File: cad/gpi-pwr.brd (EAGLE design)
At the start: 133 x 73.5 mm, 102 parts, among them CN1 HEADER-1X2, CN2 HEADER-3X1, CN3 HEADER-1X2.4, Q1 MOSFETTO247REV, Q3 MOSFETTO247REV, Q5 MOSFETTO247REV, Q6 MOSFETTO247REV, Q7 MOSFETTO247REV, Q8 MOSFETTO247REV, U1 ACS709, U10 LM61, U11 MAX4452, U12 MAX4452, U2 ACS709, U3 ACPL-P346P346, U4 ACPL-P346P346, U5 ACPL-P346P346, U6 ACPL-P346P346, U7 ACPL-P346P346, U8 ACPL-P346P346, U9 LM61

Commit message: planes
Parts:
- removed Z1: SHORT, jaw:SHORT
- added C29, C30: .1u, jaw:SMD0603
- moved C23 7.07 mm to (38.0, 12.0), turned to 180 degrees
- moved C20 1.30 mm to (80.7, 15.5)
- moved U10 1.04 mm to (80.5, 12.8)
- moved C24 0.51 mm to (38.0, 10.0)
- moved C6 0.30 mm to (112.0, 41.5)
- moved C7 0.30 mm to (112.0, 64.0)
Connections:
- removed net GNDA: C10.1, C11.1, C12.2, C19.2, C20.2, C23.2, C24.2, C25.2, C27.2, C28.2, C5.1, C8.1, C9.2, R10.2, R5.1, U1.15, U1.22, U10.3, U11.2, U12.2, U2.15, U2.22, U9.3, Z1.P$1
- removed net N$32: J2.7
- removed net N$45: J2.8
- removed net N$49: J3.8
- removed net N$53: J3.7
- net GNDM: now also C10.1, C11.1, C12.2, C19.2, C20.2, C23.2, C24.2, C25.2, C27.2, C28.2, C29.2, C30.2, C5.1, C8.1, C9.2, J2.7, J2.8, J3.7, J3.8, R10.2, R5.1, U1.15, U1.22, U10.3, U11.2, U12.2, U2.15, U2.22, U9.3; no longer Z1.P$2
- net VCC: now also C29.1, C30.1
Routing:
- net GNDA: track 115.1 -> 0.00 mm, vias 20 -> 0
- net VCC: track 195.6 -> 109.1 mm, vias 3 -> 6
- net GNDM: track 46.0 -> 128.5 mm, vias 44 -> 39
- net GND: track 100.6 -> 148.1 mm, vias 8 -> 9
- net N$4: track 133.6 -> 143.3 mm
- net V1KDC: track 146.5 -> 147.7 mm
- net ADC5: track 15.3 -> 16.3 mm, vias 0 -> 1
- net N$25: track 104.2 -> 103.3 mm, vias 8 -> 5
- net N$24: track 83.1 -> 82.5 mm
- net N$16: track 101.7 -> 102.2 mm, vias 11 -> 0
- added copper zone on layer 15, net N$4
- added copper zone on layer 15, net VCC
- removed copper zone on layer 15, net GNDA
- removed copper zone on layer 2, net GNDA

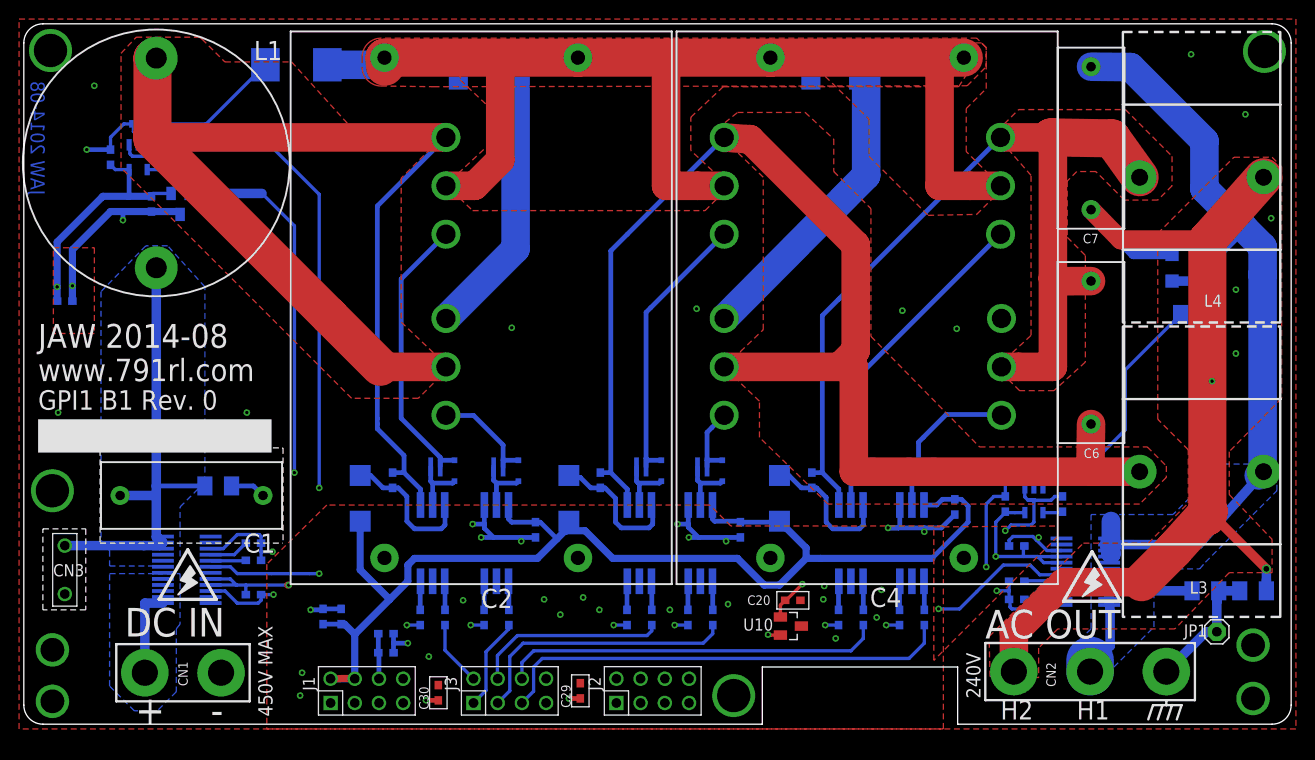
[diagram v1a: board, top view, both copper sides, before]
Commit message: output filter
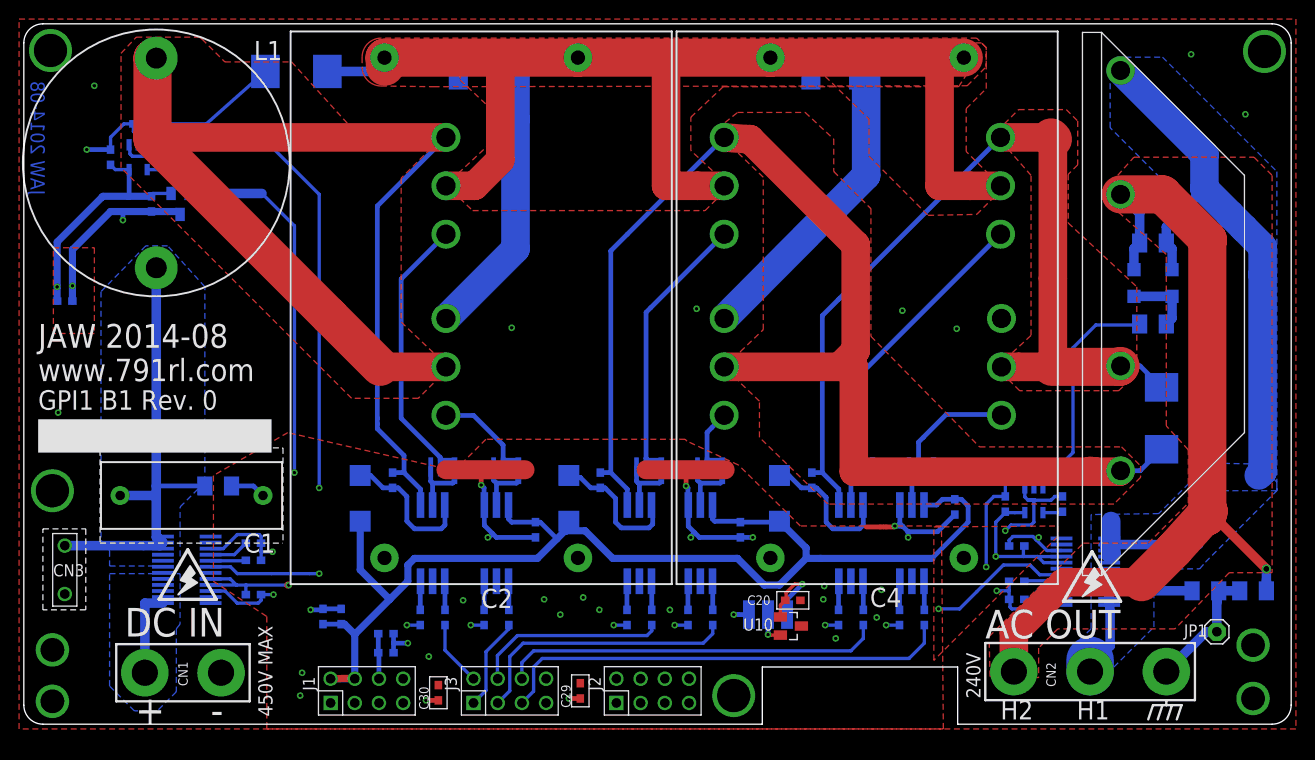
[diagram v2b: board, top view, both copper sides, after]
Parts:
- removed C7: .47u, jaw:R46KI333000N1M
- removed L3, L4: 15u, jaw:BOURNS2303
- added CN4: HEADER-3X12MM, jaw:HEADER-3X1-2SMD
- added R28: 1M, jaw:SMD1206
- added R29: 2M 2kV, jaw:SMD2512
- added Z1, Z2, Z3: SHORT, jaw:SHORT
- C6: value .47u -> FILTER; device jaw:R46KI333000N1M -> jaw-brd:FILTER-B4R0
- moved C6 8.21 mm to (115.1, 49.1)
- moved R12 4.41 mm to (118.5, 44.5)
- moved D2 4.31 mm to (116.5, 48.8)
- moved D1 4.03 mm to (120.5, 48.8)
- moved R1 0.70 mm to (28.6, 71.0)
- moved U$4 0.14 mm to (74.7, 70.8)
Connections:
- net ADC5: now also CN4.2
- net GND: now also C13.2, C15.2, C17.2, U3.VE, U5.VE, U7.VE, Z1.P$1, Z2.P$1, Z3.P$1
- net GNDM: now also CN4.3, Z1.P$2, Z2.P$2, Z3.P$2; no longer C13.2, C15.2, C17.2, U3.VE, U5.VE, U7.VE
- net N$15: now also C6.IN1, R29.P$2; no longer C6.P$1, L3.P$1
- net N$16: now also C6.IN2, R29.P$1; no longer C6.P$2, L4.P$1
- net N$24: now also C6.OUT1, R28.2; no longer C7.P$1, L3.P$2
- net N$25: now also C6.OUT2, R28.1; no longer C7.P$2, L4.P$2
- net VCC: now also CN4.1
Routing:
- net GND: track 148.1 -> 182.5 mm, vias 9 -> 15
- net N$25: track 103.3 -> 90.5 mm, vias 5 -> 1
- net N$24: track 82.5 -> 73.6 mm
- net GNDM: track 128.5 -> 122.7 mm, vias 39 -> 31
- net VCC: track 109.1 -> 113.4 mm
- net N$16: track 102.2 -> 99.2 mm
- net ADC5: track 16.3 -> 18.4 mm
- net OP2: track 26.8 -> 24.8 mm
- net N$15: track 137.6 -> 136.0 mm
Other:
- board text added: "G"
- board text added: "Pb"
- board text added: "T"
- board text added: "V"

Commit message: tweak
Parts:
- removed R29: 2M 2kV, jaw:SMD2512
- removed R3: 392k, jaw:SMD1206
- R4: value 392k -> 1M
- moved J2 15.0 mm to (51.0, 6.00)
- moved J3 15.0 mm to (66.0, 6.00)
- moved D1 7.10 mm to (113.5, 50.0)
- moved D2 7.10 mm to (109.5, 50.0)
- moved R12 7.07 mm to (111.5, 45.5)
- moved U$2 4.00 mm to (116.1, 17.5)
- moved R28 3.35 mm to (115.5, 54.5)
- moved JP1 2.62 mm to (122.7, 13.0)
- moved R4 1.08 mm to (123.0, 16.1)
- moved C6 1.00 mm to (114.1, 49.2)
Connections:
- net ADC1: now also J3.1; no longer J2.1
- net ADC2: now also J3.2; no longer J2.2
- net ADC3: now also J3.3; no longer J2.3
- net ADC4: now also J3.4; no longer J2.4
- net ADC5: now also J3.5; no longer J2.5
- net ADC6: now also J3.6; no longer J2.6
- net GATE1: now also J2.1; no longer J3.1
- net GATE2: now also J2.2; no longer J3.2
- net GATE3: now also J2.3; no longer J3.3
- net GATE4: now also J2.4; no longer J3.4
- net GATE5: now also J2.5; no longer J3.5
- net GATE6: now also J2.6; no longer J3.6
- net N$11: no longer R3.2
- net N$15: no longer R29.P$2
- net N$16: no longer R29.P$1
- net N$25: no longer R3.1
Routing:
- net N$25: track 90.5 -> 10.6 mm, vias 1 -> 0
- net N$24: track 73.6 -> 84.2 mm
- net N$15: track 136.0 -> 129.7 mm
- net N$16: track 99.2 -> 93.0 mm
- net ADC4: track 84.1 -> 88.8 mm
- net OP2: track 24.8 -> 20.3 mm
- net N$11: track 13.5 -> 9.98 mm
- net N$10: track 20.1 -> 18.7 mm
- net ADC2: track 93.4 -> 94.0 mm
- net GND: vias 15 -> 13
- added copper zone on layer 16, net GNDM
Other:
- board size 133 x 73.5 mm -> 130 x 73.5 mm
- board text added: "---"
- board text added: "DO NOT TOUCH CIRCUIT WITH REMAINING FINGER"
- board text added: "GPI1PWR Rev. 1"
- board text added: "JAW 2014-09"
- board text removed: "GPI1 B1 Rev. 0"
- board text removed: "JAW 2014-08"

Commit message: tweak
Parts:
- moved R4 1.80 mm to (121.2, 16.1)
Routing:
- net N$10: track 18.7 -> 16.9 mm
- net N$11: track 9.98 -> 9.26 mm
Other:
- board text added: "Genius hath electric power Which earth can never tame, Bright suns may scorch and dark clouds lower, Its flash is still the same. -- Lydia Maria Child"
- board text removed: "DO NOT TOUCH CIRCUIT WITH REMAINING FINGER"
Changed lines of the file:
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@@
 <layer number="14" name="Route14" color="1" fill="6" visible="no" active="no"/>
 <layer number="15" name="Signal" color="5" fill="1" visible="no" active="yes"/>
-<layer number="16" name="Bottom" color="1" fill="1" visible="yes" active="yes"/>
+<layer number="16" name="Bottom" color="1" fill="1" visible="no" active="yes"/>
 <layer number="17" name="Pads" color="2" fill="1" visible="yes" active="yes"/>
 <layer number="18" name="Vias" color="2" fill="1" visible="yes" active="yes"/>
@@
 <layer number="20" name="Dimension" color="15" fill="1" visible="yes" active="yes"/>
 <layer number="21" name="tPlace" color="7" fill="1" visible="yes" active="yes"/>
-<layer number="22" name="bPlace" color="7" fill="1" visible="no" active="yes"/>
+<layer number="22" name="bPlace" color="7" fill="1" visible="yes" active="yes"/>
 <layer number="23" name="tOrigins" color="15" fill="1" visible="yes" active="yes"/>
 <layer number="24" name="bOrigins" color="15" fill="1" visible="yes" active="yes"/>
@@
 <text x="78.4" y="16.3" size="1" layer="22" ratio="10" rot="MR0">T</text>
 <text x="76.4" y="16.3" size="1" layer="22" ratio="10" rot="MR0">G</text>
-<text x="124" y="33.2" size="3" layer="22" ratio="10" rot="MR0">Pb</text>
-<circle x="121.7" y="34.7" radius="3.306053125" width="0.25" layer="22"/>
-<wire x1="124.1" y1="37" x2="119.4" y2="32.3" width="0.25" layer="22"/>
+<text x="120.6" y="33.1" size="3" layer="22" ratio="10" rot="MR0">Pb</text>
+<circle x="118.3" y="34.5" radius="3.306053125" width="0.25" layer="22"/>
+<wire x1="120.6" y1="36.8" x2="115.9" y2="32.1" width="0.25" layer="22"/>
 <text x="114.1" y="3.1" size="1.25" layer="21" ratio="20">---</text>
-<text x="126" y="50" size="1" layer="22" ratio="10" rot="MR90">DO NOT TOUCH CIRCUIT
-WITH REMAINING FINGER</text>
 <polygon width="0.25" layer="30">
 <vertex x="20.7" y="59.4"/>
@@
 <vertex x="19.5" y="58.2"/>
 </polygon>
+<text x="130.6" y="69.2" size="1.25" layer="22" ratio="10" rot="SMR270">Genius hath electric power
+Which earth can never tame,
+Bright suns may scorch and dark clouds lower,
+Its flash is still the same.
+     -- Lydia Maria Child
+</text>
 </plain>
 <attributes>
@@
 <attribute name="VALUE" x="78.222" y="16.914" size="1" layer="27" font="vector" ratio="10"/>
 </element>
-<element name="R4" library="jaw" package="SMD1206" value="1M" x="123" y="16.1" smashed="yes" rot="MR0">
-<attribute name="NAME" x="122.37" y="17.97" size="1" layer="26" ratio="10" rot="MR0"/>
-<attribute name="VALUE" x="124.97" y="18.56" size="1.27" layer="28" rot="MR0"/>
+<element name="R4" library="jaw" package="SMD1206" value="1M" x="121.2" y="16.1" smashed="yes" rot="MR0">
+<attribute name="NAME" x="120.57" y="17.97" size="1" layer="26" ratio="10" rot="MR0"/>
+<attribute name="VALUE" x="123.17" y="18.56" size="1.27" layer="28" rot="MR0"/>
 </element>
 <element name="R19" library="jaw" package="SMD0508" value="4r7" x="64.8" y="29.5" smashed="yes" rot="MR0">
@@
 <wire x1="114" y1="14.3325" x2="113.9" y2="15.6425" width="1" layer="16"/>
 <wire x1="113.9175" y1="15.7" x2="113.9" y2="16.9125" width="1" layer="16"/>
-<wire x1="121.6" y1="16.1" x2="113.8975" y2="16.1" width="1" layer="16"/>
+<wire x1="119.8" y1="16.1" x2="113.8975" y2="16.1" width="1" layer="16"/>
 <wire x1="113.8975" y1="16.1" x2="113.9" y2="15.0075" width="1" layer="16"/>
 <polygon width="0.2" layer="16" thermals="no">
@@
 <contactref element="CN2" pad="P$2"/>
 <contactref element="R4" pad="1"/>
-<wire x1="122.7" y1="13" x2="124.4" y2="14.7" width="1" layer="16"/>
-<wire x1="124.4" y1="14.7" x2="124.4" y2="16.1" width="1" layer="16"/>
-<wire x1="122.7" y1="13" x2="122.78" y2="10.9" width="1" layer="16"/>
-<wire x1="122.78" y1="10.9" x2="119.9" y2="8.02" width="1" layer="16"/>
+<wire x1="122.7" y1="13" x2="122.7" y2="15.9" width="1" layer="16"/>
+<wire x1="122.7" y1="15.9" x2="122.6" y2="16.1" width="1" layer="16"/>
+<wire x1="122.7" y1="13" x2="122.68" y2="10.8" width="1" layer="16"/>
+<wire x1="122.68" y1="10.8" x2="119.9" y2="8.02" width="1" layer="16"/>
 </signal>
 <signal name="N$7">
@@
 <signal name="N$33">
 <via x="127" y="73" extent="1-16" drill="3.5"/>
+<via x="127" y="16" extent="1-16" drill="3.5"/>
+<wire x1="127" y1="16" x2="127" y2="73" width="0" layer="19" extent="1-1"/>
 </signal>
 <signal name="N$2">

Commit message: tweak
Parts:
- moved U$7 1.30 mm to (117.1, 13.5)
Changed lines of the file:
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@@
 <layer number="14" name="Route14" color="1" fill="6" visible="no" active="no"/>
 <layer number="15" name="Signal" color="5" fill="1" visible="no" active="yes"/>
-<layer number="16" name="Bottom" color="1" fill="1" visible="no" active="yes"/>
+<layer number="16" name="Bottom" color="1" fill="1" visible="yes" active="yes"/>
 <layer number="17" name="Pads" color="2" fill="1" visible="yes" active="yes"/>
 <layer number="18" name="Vias" color="2" fill="1" visible="yes" active="yes"/>
 <layer number="19" name="Unrouted" color="6" fill="1" visible="yes" active="yes"/>
 <layer number="20" name="Dimension" color="15" fill="1" visible="yes" active="yes"/>
-<layer number="21" name="tPlace" color="7" fill="1" visible="yes" active="yes"/>
+<layer number="21" name="tPlace" color="7" fill="1" visible="no" active="yes"/>
 <layer number="22" name="bPlace" color="7" fill="1" visible="yes" active="yes"/>
 <layer number="23" name="tOrigins" color="15" fill="1" visible="yes" active="yes"/>
 <layer number="24" name="bOrigins" color="15" fill="1" visible="yes" active="yes"/>
 <layer number="25" name="tNames" color="7" fill="1" visible="no" active="yes"/>
-<layer number="26" name="bNames" color="7" fill="1" visible="no" active="yes"/>
+<layer number="26" name="bNames" color="7" fill="1" visible="yes" active="yes"/>
 <layer number="27" name="tValues" color="7" fill="1" visible="no" active="yes"/>
 <layer number="28" name="bValues" color="7" fill="1" visible="no" active="yes"/>
 <layer number="29" name="tStop" color="7" fill="3" visible="no" active="yes"/>
-<layer number="30" name="bStop" color="7" fill="6" visible="yes" active="yes"/>
+<layer number="30" name="bStop" color="7" fill="6" visible="no" active="yes"/>
 <layer number="31" name="tCream" color="7" fill="4" visible="no" active="yes"/>
 <layer number="32" name="bCream" color="7" fill="5" visible="no" active="yes"/>
@@
 <vertex x="19.5" y="58.2"/>
 </polygon>
-<text x="130.6" y="69.2" size="1.25" layer="22" ratio="10" rot="SMR270">Genius hath electric power
+<text x="131" y="69.5" size="1.25" layer="22" ratio="10" rot="SMR270">Genius hath electric power
 Which earth can never tame,
-Bright suns may scorch and dark clouds lower,
+Bright suns may scorch and
+dark clouds lower,
 Its flash is still the same.
      -- Lydia Maria Child
@@
 </class>
 </classes>
-<designrules name="LaenPCBOrder *">
+<designrules name="OSHPark-4layer (1)">
 <description language="de">&lt;b&gt;EAGLE Design Rules&lt;/b&gt;
 &lt;p&gt;
@@
 Please make sure your boards conform to these design rules.</description>
 <param name="layerSetup" value="(1*2*15*16)"/>
-<param name="mtCopper" value="0.0356mm 0.0356mm 0.0356mm 0.0356mm 0.0356mm 0.0356mm 0.0356mm 0.0356mm 0.0356mm 0.0356mm 0.0356mm 0.0356mm 0.0356mm 0.0356mm 0.0356mm 0.0356mm"/>
-<param name="mtIsolate" value="1.5011mm 0.1499mm 0.2007mm 0.1499mm 0.2007mm 0.1499mm 0.2007mm 0.1499mm 0.2007mm 0.1499mm 0.2007mm 0.1499mm 0.2007mm 0.1499mm 0.2007mm"/>
-<param name="mdWireWire" value="6mil"/>
-<param name="mdWirePad" value="6mil"/>
-<param name="mdWireVia" value="6mil"/>
-<param name="mdPadPad" value="6mil"/>
-<param name="mdPadVia" value="6mil"/>
-<param name="mdViaVia" value="6mil"/>
-<param name="mdSmdPad" value="6mil"/>
-<param name="mdSmdVia" value="6mil"/>
-<param name="mdSmdSmd" value="6mil"/>
+<param name="mtCopper" value="0.035559375mm 0.01778125mm 0.0356mm 0.0356mm 0.0356mm 0.0356mm 0.0356mm 0.0356mm 0.0356mm 0.0356mm 0.0356mm 0.0356mm 0.0356mm 0.0356mm 0.01778125mm 0.035559375mm"/>
+<param name="mtIsolate" value="0.17018125mm 47mil 0.2007mm 0.1499mm 0.2007mm 0.1499mm 0.2007mm 0.1499mm 0.2007mm 0.1499mm 0.2007mm 0.1499mm 0.2007mm 0.1499mm 0.17018125mm"/>
+<param name="mdWireWire" value="5mil"/>
+<param name="mdWirePad" value="5mil"/>
+<param name="mdWireVia" value="5mil"/>
+<param name="mdPadPad" value="5mil"/>
+<param name="mdPadVia" value="5mil"/>
+<param name="mdViaVia" value="5mil"/>
+<param name="mdSmdPad" value="5mil"/>
+<param name="mdSmdVia" value="5mil"/>
+<param name="mdSmdSmd" value="5mil"/>
 <param name="mdViaViaSameLayer" value="8mil"/>
 <param name="mnLayersViaInSmd" value="2"/>
@@
 <param name="mdDrill" value="6mil"/>
 <param name="mdSmdStop" value="0mil"/>
-<param name="msWidth" value="6mil"/>
-<param name="msDrill" value="13mil"/>
-<param name="msMicroVia" value="13mil"/>
+<param name="msWidth" value="5mil"/>
+<param name="msDrill" value="10mil"/>
+<param name="msMicroVia" value="10mil"/>
 <param name="msBlindViaRatio" value="0.5"/>
 <param name="rvPadTop" value="0.25"/>
@@
 <param name="rvMicroViaOuter" value="0.25"/>
 <param name="rvMicroViaInner" value="0.25"/>
-<param name="rlMinPadTop" value="7mil"/>
+<param name="rlMinPadTop" value="4mil"/>
 <param name="rlMaxPadTop" value="20mil"/>
-<param name="rlMinPadInner" value="7mil"/>
+<param name="rlMinPadInner" value="4mil"/>
 <param name="rlMaxPadInner" value="20mil"/>
-<param name="rlMinPadBottom" value="7mil"/>
+<param name="rlMinPadBottom" value="4mil"/>
 <param name="rlMaxPadBottom" value="20mil"/>
-<param name="rlMinViaOuter" value="7mil"/>
+<param name="rlMinViaOuter" value="4mil"/>
 <param name="rlMaxViaOuter" value="20mil"/>
-<param name="rlMinViaInner" value="7mil"/>
+<param name="rlMinViaInner" value="4mil"/>
 <param name="rlMaxViaInner" value="20mil"/>
 <param name="rlMinMicroViaOuter" value="4mil"/>
@@
 <param name="mlMinCreamFrame" value="0mil"/>
 <param name="mlMaxCreamFrame" value="0mil"/>
-<param name="mlViaStopLimit" value="0.35mm"/>
+<param name="mlViaStopLimit" value="0mil"/>
 <param name="srRoundness" value="0"/>
 <param name="srMinRoundness" value="0mil"/>
@@
 </element>
 <element name="Q1" library="jaw" package="TO-247-3-DOWN" value="MOSFETTO247REV" x="44.3" y="40" smashed="yes" rot="MR0">
-<attribute name="NAME" x="23.98" y="46.35" size="2.54" layer="26" rot="MR270"/>
+<attribute name="NAME" x="30.88" y="47.55" size="2.54" layer="26" rot="MR270"/>
 </element>
 <element name="Q3" library="jaw" package="TO-247-3-DOWN" value="MOSFETTO247REV" x="44.3" y="59" smashed="yes" rot="MR0">
@@
 <element name="U$5" library="jaw" package="SYMBOL-WARNING" value="SYMBOL-WARNING" x="14.1" y="31.5" rot="MR90"/>
 <element name="U$6" library="jaw" package="SYMBOL-WARNING" value="SYMBOL-WARNING" x="8.4" y="14.2" rot="MR0"/>
-<element name="U$7" library="jaw" package="SYMBOL-WARNING" value="SYMBOL-WARNING" x="118.3" y="14" rot="MR0"/>
+<element name="U$7" library="jaw" package="SYMBOL-WARNING" value="SYMBOL-WARNING" x="117.1" y="13.5" rot="MR0"/>
 <element name="C26" library="jaw" package="SMD2220" value=".1u" x="48.1" y="71.6" smashed="yes" rot="MR180">
 <attribute name="NAME" x="39.9" y="69.9" size="1.27" layer="26" ratio="10" rot="MR180"/>
